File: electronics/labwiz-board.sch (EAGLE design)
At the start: 98 parts, among them J1 SD_MICRO_SDIO_1BIT, J2 CORTEX_DEBUGSMD_original, U1 STM32F10XRXT6, U2 MCP73831/2, U4 MIC5219-3.3V, X2 M12_BOTTOM_CONTACTS_FPC_1MM, Y3 32.768kHz

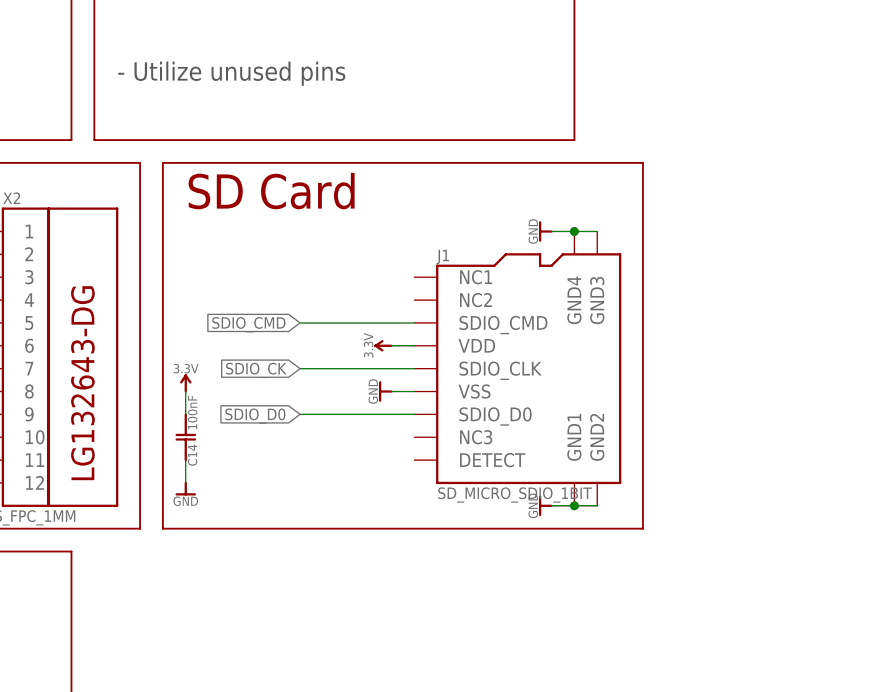
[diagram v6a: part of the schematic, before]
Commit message: Added pullups to the SD interface. Closes #24.
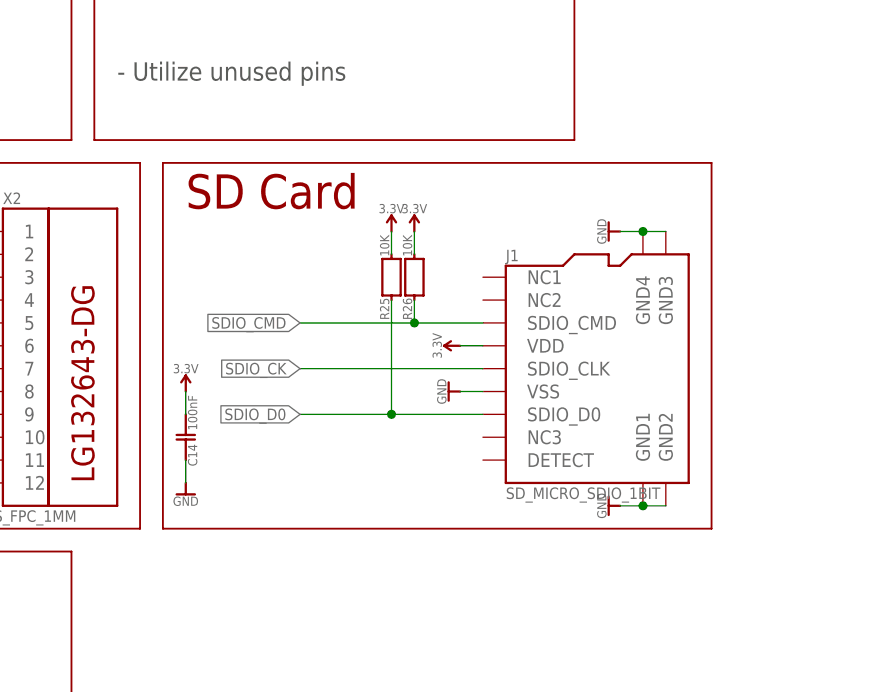
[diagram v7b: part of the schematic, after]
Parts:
- added R25, R26: 10K, PaxInstruments-RCL:RESISTOR_FIXED_10K_0402
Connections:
- net 3.3V: now also R25.1, R26.1
- net SDIO_CMD: now also R26.2
- net SDIO_D0: now also R25.2
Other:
- moved on the sheet: J1
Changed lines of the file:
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@@
 <part name="SUPPLY12" library="PaxInstruments-Aesthetics" deviceset="SYM_VCC" device="" technology="3.3V" value="3.3V"/>
 <part name="SUPPLY19" library="PaxInstruments-Aesthetics" deviceset="SYM_VCC" device="" technology="3.3V" value="3.3V"/>
+<part name="R25" library="PaxInstruments-RCL" deviceset="RESISTOR_FIXED" device="_0402" technology="_10K" value="10K">
+<attribute name="MPN" value=""/>
+<attribute name="POPULATE" value=""/>
+</part>
+<part name="R26" library="PaxInstruments-RCL" deviceset="RESISTOR_FIXED" device="_0402" technology="_10K" value="10K">
+<attribute name="MPN" value=""/>
+<attribute name="POPULATE" value=""/>
+</part>
+<part name="SUPPLY20" library="PaxInstruments-Aesthetics" deviceset="SYM_VCC" device="" technology="3.3V" value="3.3V"/>
+<part name="SUPPLY21" library="PaxInstruments-Aesthetics" deviceset="SYM_VCC" device="" technology="3.3V" value="3.3V"/>
 </parts>
 <sheets>
@@
 <text x="190.5" y="83.82" size="3.81" layer="94">Buttons</text>
 <text x="330.2" y="15.24" size="2.54" layer="94" align="center-left">0.3</text>
-<wire x1="297.18" y1="88.9" x2="350.52" y2="88.9" width="0.2032" layer="94"/>
+<wire x1="297.18" y1="88.9" x2="358.14" y2="88.9" width="0.2032" layer="94"/>
 <wire x1="297.18" y1="88.9" x2="297.18" y2="48.26" width="0.2032" layer="94"/>
-<wire x1="350.52" y1="88.9" x2="350.52" y2="48.26" width="0.2032" layer="94"/>
-<wire x1="297.18" y1="48.26" x2="350.52" y2="48.26" width="0.2032" layer="94"/>
+<wire x1="358.14" y1="88.9" x2="358.14" y2="48.26" width="0.2032" layer="94"/>
+<wire x1="297.18" y1="48.26" x2="358.14" y2="48.26" width="0.2032" layer="94"/>
 <text x="330.2" y="5.08" size="2.54" layer="94" align="center-left">Charles Pax</text>
 <text x="299.72" y="83.82" size="3.81" layer="94">SD Card</text>
@@
 <attribute name="MF" x="15.24" y="238.76" size="1.778" layer="96" display="off"/>
 </instance>
-<instance part="J1" gate="G$1" x="327.66" y="53.34">
-<attribute name="MF" x="327.66" y="53.34" size="1.778" layer="96" display="off"/>
-</instance>
-<instance part="GND11" gate="G$1" x="322.58" y="63.5" rot="R270"/>
+<instance part="J1" gate="G$1" x="335.28" y="53.34">
+<attribute name="MF" x="335.28" y="53.34" size="1.778" layer="96" display="off"/>
+</instance>
+<instance part="GND11" gate="G$1" x="330.2" y="63.5" rot="R270"/>
 <instance part="C14" gate="G$1" x="299.72" y="58.42" rot="MR0"/>
 <instance part="U1" gate="PORTA_L" x="17.78" y="73.66" rot="MR0"/>
@@
 <instance part="GND38" gate="G$1" x="264.16" y="53.34" rot="R270"/>
 <instance part="P+5" gate="G$1" x="274.32" y="83.82"/>
-<instance part="GND22" gate="G$1" x="340.36" y="50.8" rot="R270"/>
-<instance part="GND32" gate="G$1" x="340.36" y="81.28" rot="R270"/>
+<instance part="GND22" gate="G$1" x="347.98" y="50.8" rot="R270"/>
+<instance part="GND32" gate="G$1" x="347.98" y="81.28" rot="R270"/>
 <instance part="GND7" gate="G$1" x="264.16" y="81.28" rot="R270"/>
 <instance part="GND39" gate="G$1" x="264.16" y="73.66" rot="R270"/>
@@
 <instance part="SUPPLY1" gate="G$1" x="48.26" y="137.16"/>
 <instance part="GND9" gate="G$1" x="48.26" y="127"/>
-<instance part="SUPPLY6" gate="G$1" x="322.58" y="68.58" rot="MR270"/>
+<instance part="SUPPLY6" gate="G$1" x="330.2" y="68.58" rot="MR270"/>
 <instance part="GND15" gate="G$1" x="228.6" y="203.2" rot="R90"/>
 <instance part="GND24" gate="G$1" x="228.6" y="228.6" rot="R90"/>
@@
 <instance part="SUPPLY12" gate="G$1" x="205.74" y="119.38"/>
 <instance part="SUPPLY19" gate="G$1" x="200.66" y="119.38"/>
+<instance part="R25" gate="G$1" x="322.58" y="76.2">
+<attribute name="MPN" x="322.58" y="76.2" size="1.778" layer="96" display="off"/>
+<attribute name="POPULATE" x="322.58" y="76.2" size="1.778" layer="96" display="off"/>
+</instance>
+<instance part="R26" gate="G$1" x="325.12" y="76.2">
+<attribute name="MPN" x="325.12" y="76.2" size="1.778" layer="96" display="off"/>
+<attribute name="POPULATE" x="325.12" y="76.2" size="1.778" layer="96" display="off"/>
+</instance>
+<instance part="SUPPLY20" gate="G$1" x="322.58" y="81.28" rot="MR0"/>
+<instance part="SUPPLY21" gate="G$1" x="325.12" y="81.28" rot="MR0"/>
 </instances>
 <busses>
@@
 <pinref part="SUPPLY6" gate="G$1" pin="3.3V"/>
 <pinref part="J1" gate="G$1" pin="VDD"/>
-<wire x1="325.12" y1="68.58" x2="322.58" y2="68.58" width="0.1524" layer="91"/>
+<wire x1="332.74" y1="68.58" x2="330.2" y2="68.58" width="0.1524" layer="91"/>
 </segment>
 <segment>
@@
 <pinref part="SUPPLY12" gate="G$1" pin="3.3V"/>
 <wire x1="205.74" y1="116.84" x2="205.74" y2="119.38" width="0.1524" layer="91"/>
+</segment>
+<segment>
+<pinref part="SUPPLY20" gate="G$1" pin="3.3V"/>
+<pinref part="R25" gate="G$1" pin="1"/>
+<wire x1="322.58" y1="81.28" x2="322.58" y2="78.74" width="0.1524" layer="91"/>
+</segment>
+<segment>
+<pinref part="SUPPLY21" gate="G$1" pin="3.3V"/>
+<pinref part="R26" gate="G$1" pin="1"/>
+<wire x1="325.12" y1="81.28" x2="325.12" y2="78.74" width="0.1524" layer="91"/>
 </segment>
 </net>
@@
 <pinref part="J1" gate="G$1" pin="GND4"/>
 <pinref part="J1" gate="G$1" pin="GND3"/>
-<wire x1="345.44" y1="81.28" x2="342.9" y2="81.28" width="0.1524" layer="91"/>
-<wire x1="342.9" y1="81.28" x2="340.36" y2="81.28" width="0.1524" layer="91"/>
-<junction x="342.9" y="81.28"/>
+<wire x1="353.06" y1="81.28" x2="350.52" y2="81.28" width="0.1524" layer="91"/>
+<wire x1="350.52" y1="81.28" x2="347.98" y2="81.28" width="0.1524" layer="91"/>
+<junction x="350.52" y="81.28"/>
 <pinref part="GND32" gate="G$1" pin="GND"/>
 </segment>
@@
 <pinref part="J1" gate="G$1" pin="GND1"/>
 <pinref part="J1" gate="G$1" pin="GND2"/>
-<wire x1="345.44" y1="50.8" x2="342.9" y2="50.8" width="0.1524" layer="91"/>
-<wire x1="342.9" y1="50.8" x2="340.36" y2="50.8" width="0.1524" layer="91"/>
-<junction x="342.9" y="50.8"/>
+<wire x1="353.06" y1="50.8" x2="350.52" y2="50.8" width="0.1524" layer="91"/>
+<wire x1="350.52" y1="50.8" x2="347.98" y2="50.8" width="0.1524" layer="91"/>
+<junction x="350.52" y="50.8"/>
 <pinref part="GND22" gate="G$1" pin="GND"/>
 </segment>
 <segment>
 <pinref part="GND11" gate="G$1" pin="GND"/>
-<wire x1="325.12" y1="63.5" x2="322.58" y2="63.5" width="0.1524" layer="91"/>
+<wire x1="332.74" y1="63.5" x2="330.2" y2="63.5" width="0.1524" layer="91"/>
 <pinref part="J1" gate="G$1" pin="VSS"/>
 </segment>
@@
 <segment>
 <pinref part="J1" gate="G$1" pin="SDIO_D0"/>
-<wire x1="325.12" y1="60.96" x2="312.42" y2="60.96" width="0.1524" layer="91"/>
+<wire x1="332.74" y1="60.96" x2="322.58" y2="60.96" width="0.1524" layer="91"/>
 <label x="312.42" y="60.96" size="1.27" layer="95" rot="R180" xref="yes"/>
+<pinref part="R25" gate="G$1" pin="2"/>
+<wire x1="322.58" y1="60.96" x2="312.42" y2="60.96" width="0.1524" layer="91"/>
+<wire x1="322.58" y1="73.66" x2="322.58" y2="60.96" width="0.1524" layer="91"/>
+<junction x="322.58" y="60.96"/>
 </segment>
 <segment>
@@
 <segment>
 <pinref part="J1" gate="G$1" pin="SDIO_CMD"/>
+<wire x1="332.74" y1="71.12" x2="325.12" y2="71.12" width="0.1524" layer="91"/>
+<label x="312.42" y="71.12" size="1.27" layer="95" rot="R180" xref="yes"/>
+<pinref part="R26" gate="G$1" pin="2"/>
 <wire x1="325.12" y1="71.12" x2="312.42" y2="71.12" width="0.1524" layer="91"/>
-<label x="312.42" y="71.12" size="1.27" layer="95" rot="R180" xref="yes"/>
+<wire x1="325.12" y1="73.66" x2="325.12" y2="71.12" width="0.1524" layer="91"/>
+<junction x="325.12" y="71.12"/>
 </segment>
 <segment>
@@
 <segment>
 <pinref part="J1" gate="G$1" pin="SDIO_CLK"/>
-<wire x1="325.12" y1="66.04" x2="312.42" y2="66.04" width="0.1524" layer="91"/>
+<wire x1="332.74" y1="66.04" x2="312.42" y2="66.04" width="0.1524" layer="91"/>
 <label x="312.42" y="66.04" size="1.27" layer="95" rot="R180" xref="yes"/>
 </segment>

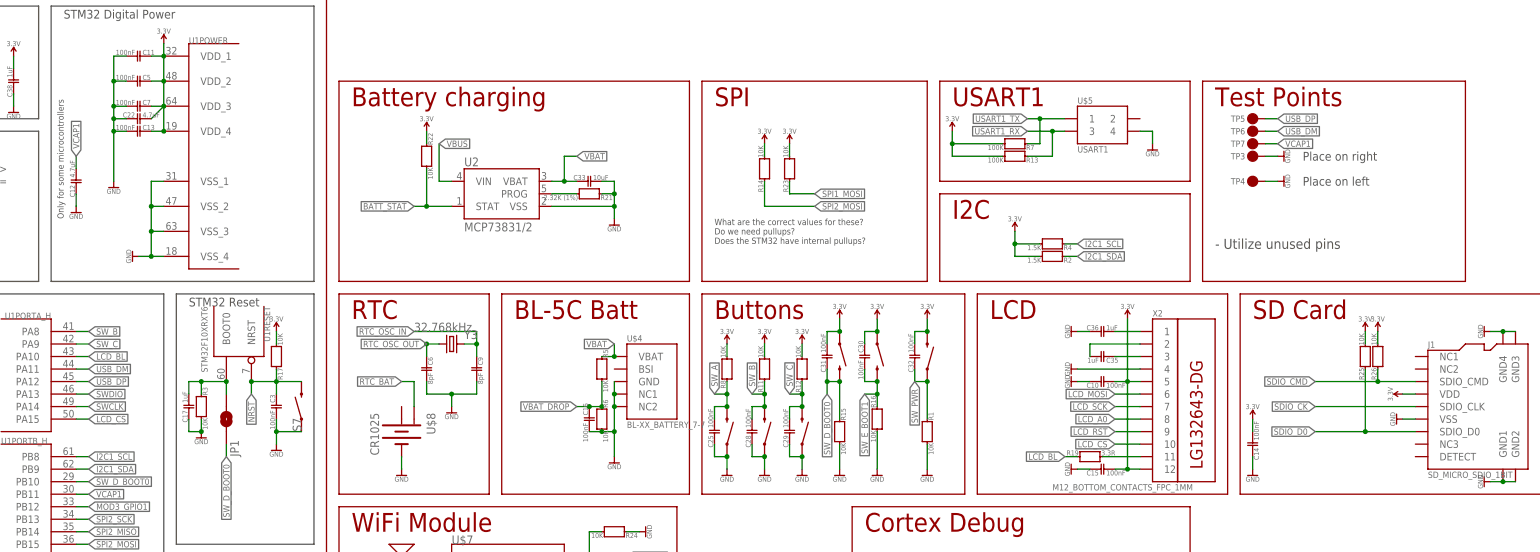
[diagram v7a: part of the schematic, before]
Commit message: Added and LED on LCD_BL for testing.
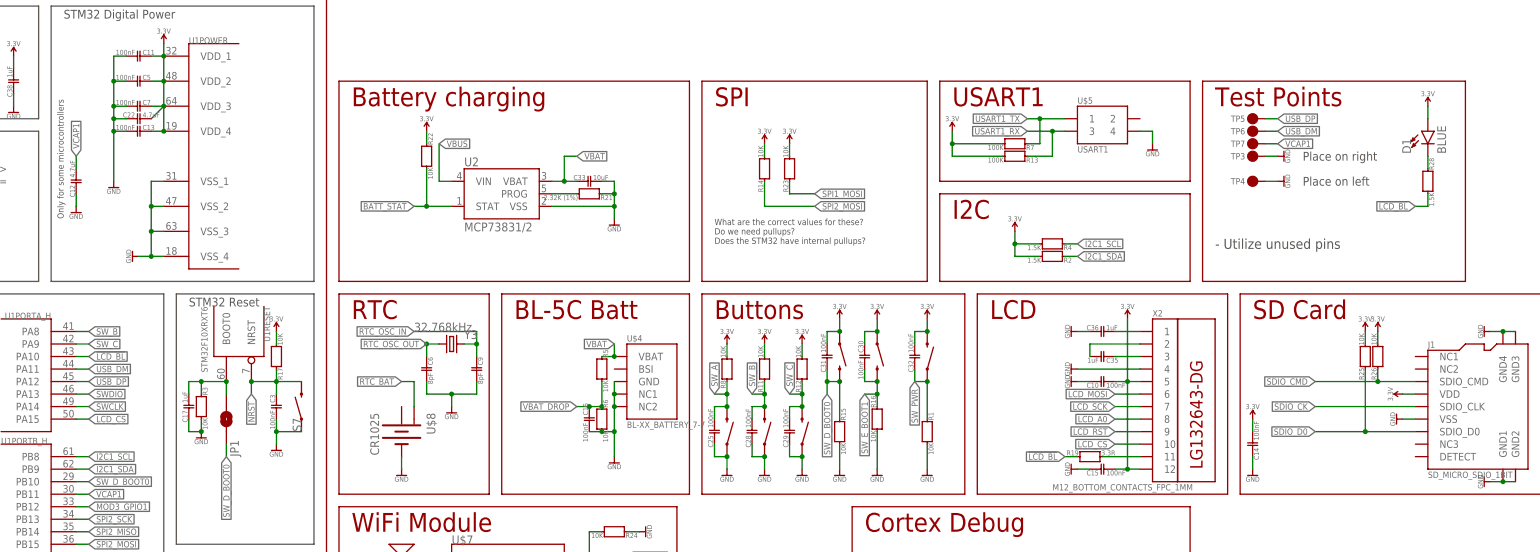
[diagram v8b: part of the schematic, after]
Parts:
- added D1: BLUE, SparkFun-LED:LED-BLUE0603
- added R28: 1.5K, PaxInstruments-RCL:RESISTOR_FIXED_1.5K_0402
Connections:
- removed net LCD_BL: R19.2, U1PORTA_H.PA10
- new net !LCD_BL: R19.2, R28.1, U1PORTA_H.PA10
- new net N$25: D1.C, R28.2
- net 3.3V: now also D1.A
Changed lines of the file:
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@@
 <part name="SUPPLY20" library="PaxInstruments-Aesthetics" deviceset="SYM_VCC" device="" technology="3.3V" value="3.3V"/>
 <part name="SUPPLY21" library="PaxInstruments-Aesthetics" deviceset="SYM_VCC" device="" technology="3.3V" value="3.3V"/>
+<part name="D1" library="SparkFun-LED" deviceset="LED-BLUE" device="0603" value="BLUE"/>
+<part name="R28" library="PaxInstruments-RCL" deviceset="RESISTOR_FIXED" device="_0402" technology="_1.5K" value="1.5K"/>
+<part name="SUPPLY22" library="PaxInstruments-Aesthetics" deviceset="SYM_VCC" device="" technology="3.3V" value="3.3V"/>
 </parts>
 <sheets>
@@
 <instance part="SUPPLY20" gate="G$1" x="322.58" y="81.28" rot="MR0"/>
 <instance part="SUPPLY21" gate="G$1" x="325.12" y="81.28" rot="MR0"/>
+<instance part="D1" gate="G$1" x="335.28" y="121.92"/>
+<instance part="R28" gate="G$1" x="335.28" y="111.76" rot="R180"/>
+<instance part="SUPPLY22" gate="G$1" x="335.28" y="127" rot="MR0"/>
 </instances>
 <busses>
@@
 <wire x1="325.12" y1="81.28" x2="325.12" y2="78.74" width="0.1524" layer="91"/>
 </segment>
+<segment>
+<pinref part="D1" gate="G$1" pin="A"/>
+<pinref part="SUPPLY22" gate="G$1" pin="3.3V"/>
+<wire x1="335.28" y1="124.46" x2="335.28" y2="127" width="0.1524" layer="91"/>
+</segment>
 </net>
 <net name="GND" class="5">
@@
 </segment>
 </net>
-<net name="LCD_BL" class="0">
+<net name="!LCD_BL" class="0">
 <segment>
 <pinref part="R19" gate="G$1" pin="2"/>
@@
 <wire x1="60.96" y1="76.2" x2="63.5" y2="76.2" width="0.1524" layer="91"/>
 <label x="63.5" y="76.2" size="1.27" layer="95" xref="yes"/>
+</segment>
+<segment>
+<pinref part="R28" gate="G$1" pin="1"/>
+<wire x1="335.28" y1="109.22" x2="335.28" y2="106.68" width="0.1524" layer="91"/>
+<wire x1="335.28" y1="106.68" x2="332.74" y2="106.68" width="0.1524" layer="91"/>
+<label x="332.74" y="106.68" size="1.27" layer="95" rot="R180" xref="yes"/>
 </segment>
 </net>
@@
 </segment>
 </net>
+<net name="N$25" class="0">
+<segment>
+<pinref part="D1" gate="G$1" pin="C"/>
+<pinref part="R28" gate="G$1" pin="2"/>
+<wire x1="335.28" y1="116.84" x2="335.28" y2="114.3" width="0.1524" layer="91"/>
+</segment>
+</net>
